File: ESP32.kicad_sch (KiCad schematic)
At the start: 16 parts, among them J24 Conn_01x02_Pin, J25 Conn_01x04_Pin, J26 Conn_01x02_Pin, J27 TC0203620000G, SW1 SW_Omron_B3FS, U2 ESP32-C3-WROOM-02

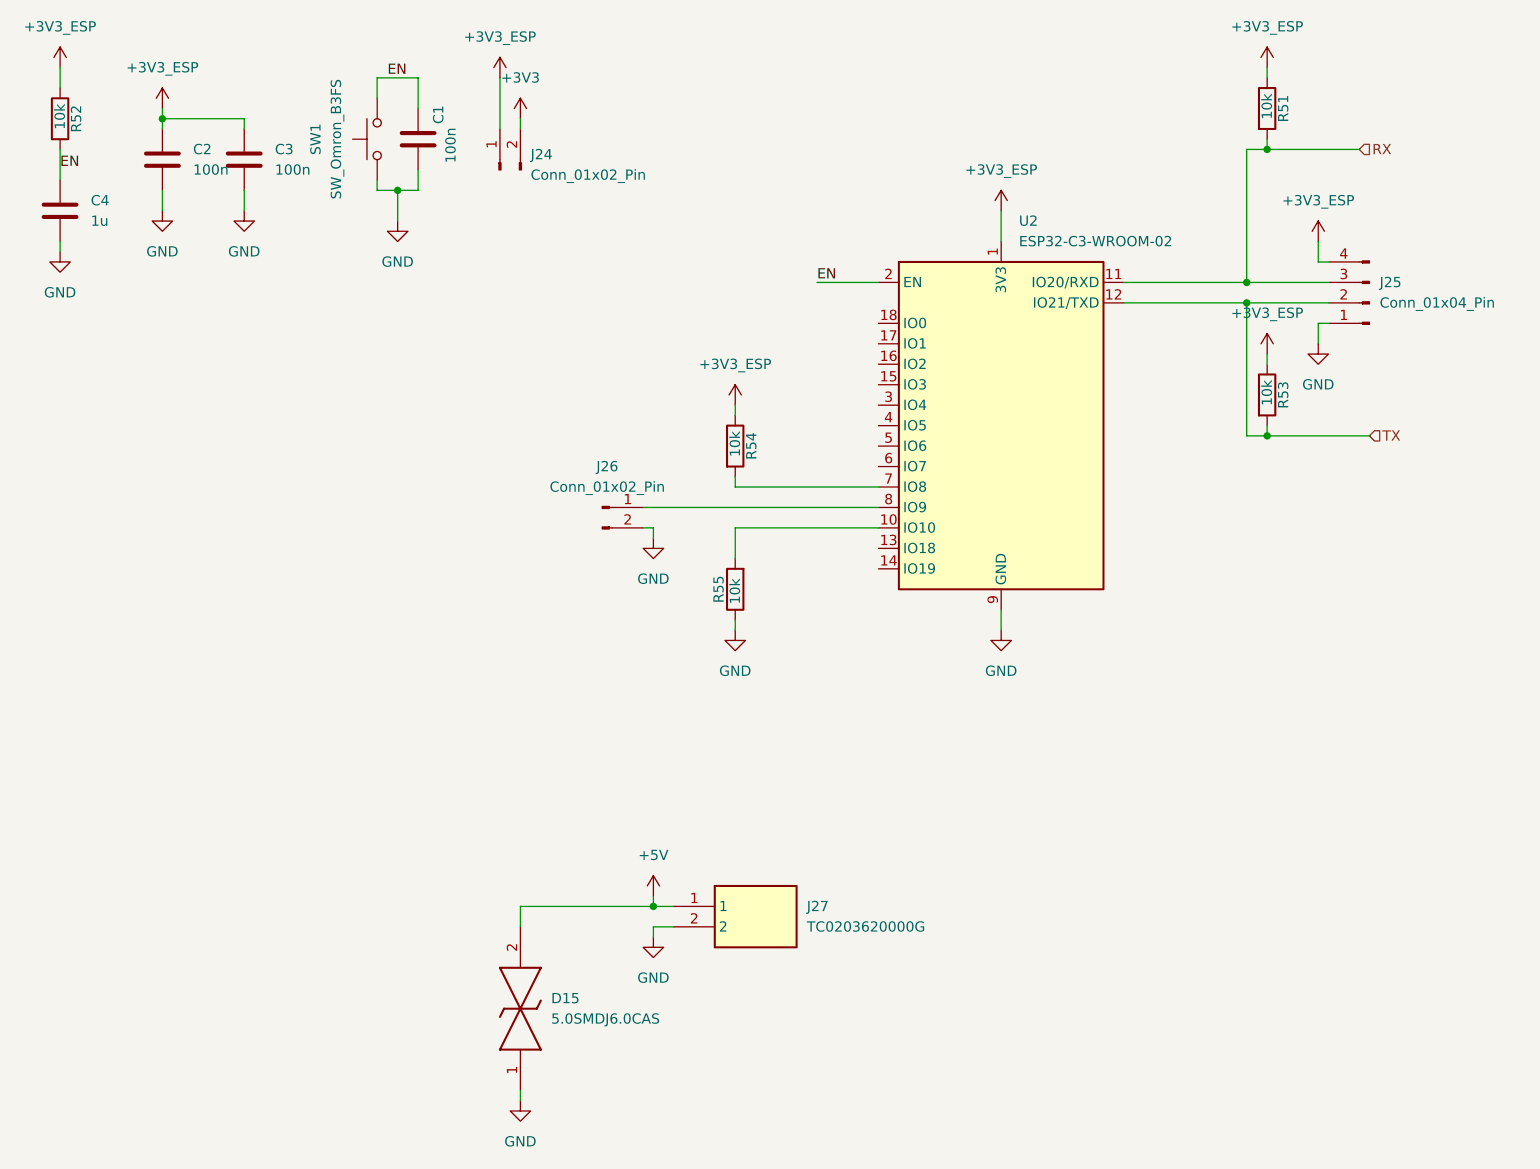
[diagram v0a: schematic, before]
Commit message: relay placment
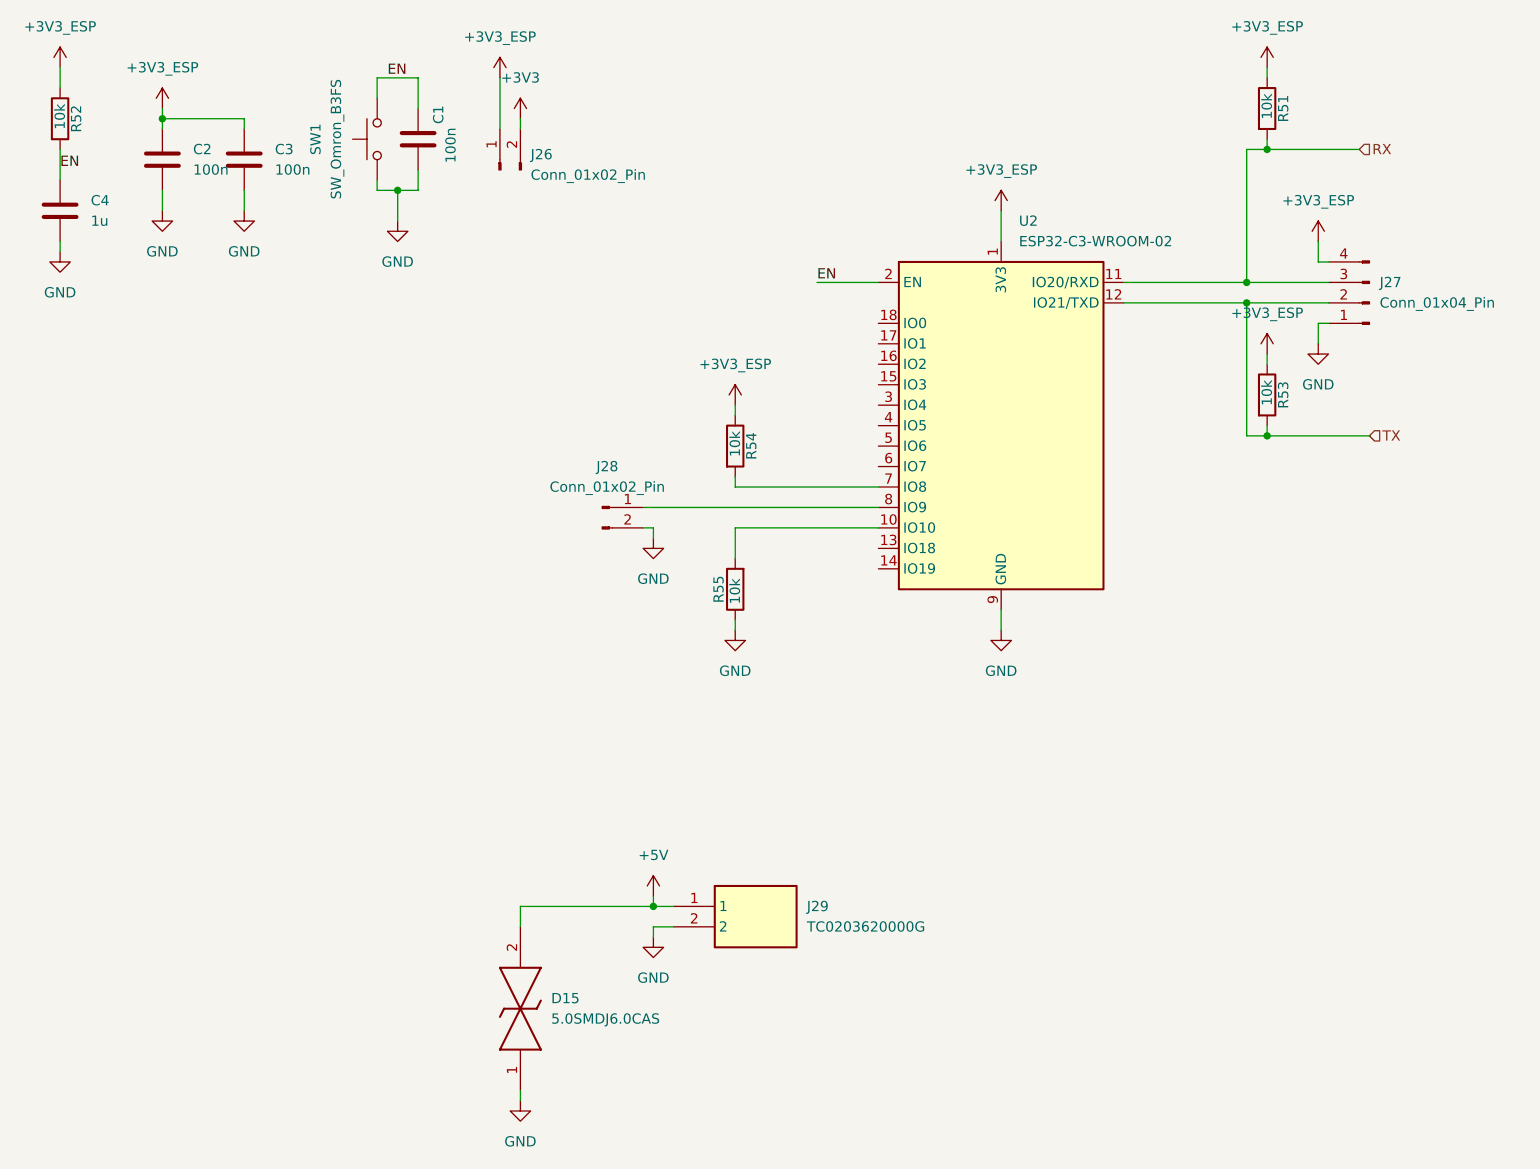
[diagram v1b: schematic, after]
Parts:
- renumbered J24 to J26, J25 to J27, J26 to J28, J27 to J29
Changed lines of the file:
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@@
 		(dnp no)
 		(fields_autoplaced yes)
-		(property "Reference" "J25"
+		(property "Reference" "J27"
 			(at 185.42 48.2599 0)
 			(effects
@@
 			(project ""
 				(path "/68de2dd7-8f08-479b-94c5-c7847794fd33/52852d8d-0d14-4226-9b6c-d04fc3c95df9"
-					(reference "J25")
+					(reference "J27")
 					(unit 1)
 				)
@@
 		(dnp no)
 		(fields_autoplaced yes)
-		(property "Reference" "#PWR0143"
+		(property "Reference" "#PWR0114"
 			(at 95.25 86.36 0)
 			(effects
@@
 			(project "home_auto"
 				(path "/68de2dd7-8f08-479b-94c5-c7847794fd33/52852d8d-0d14-4226-9b6c-d04fc3c95df9"
-					(reference "#PWR0143")
+					(reference "#PWR0114")
 					(unit 1)
 				)
@@
 		(dnp no)
 		(fields_autoplaced yes)
-		(property "Reference" "#PWR0145"
+		(property "Reference" "#PWR0116"
 			(at 138.43 97.79 0)
 			(effects
@@
 			(project "home_auto"
 				(path "/68de2dd7-8f08-479b-94c5-c7847794fd33/52852d8d-0d14-4226-9b6c-d04fc3c95df9"
-					(reference "#PWR0145")
+					(reference "#PWR0116")
 					(unit 1)
 				)
@@
 		(dnp no)
 		(fields_autoplaced yes)
-		(property "Reference" "#PWR0139"
+		(property "Reference" "#PWR0110"
 			(at 21.59 50.8 0)
 			(effects
@@
 			(project "home_auto"
 				(path "/68de2dd7-8f08-479b-94c5-c7847794fd33/52852d8d-0d14-4226-9b6c-d04fc3c95df9"
-					(reference "#PWR0139")
+					(reference "#PWR0110")
 					(unit 1)
 				)
@@
 		(dnp no)
 		(fields_autoplaced yes)
-		(property "Reference" "#PWR0129"
+		(property "Reference" "#PWR0100"
 			(at 21.59 25.4 0)
 			(effects
@@
 			(project "home_auto"
 				(path "/68de2dd7-8f08-479b-94c5-c7847794fd33/52852d8d-0d14-4226-9b6c-d04fc3c95df9"
-					(reference "#PWR0129")
+					(reference "#PWR0100")
 					(unit 1)
 				)
@@
 		(dnp no)
 		(fields_autoplaced yes)
-		(property "Reference" "#PWR0137"
+		(property "Reference" "#PWR0108"
 			(at 63.5 46.99 0)
 			(effects
@@
 			(project "home_auto"
 				(path "/68de2dd7-8f08-479b-94c5-c7847794fd33/52852d8d-0d14-4226-9b6c-d04fc3c95df9"
-					(reference "#PWR0137")
+					(reference "#PWR0108")
 					(unit 1)
 				)
@@
 		(dnp no)
 		(fields_autoplaced yes)
-		(property "Reference" "#PWR0142"
+		(property "Reference" "#PWR0113"
 			(at 105.41 67.31 0)
 			(effects
@@
 			(project "home_auto"
 				(path "/68de2dd7-8f08-479b-94c5-c7847794fd33/52852d8d-0d14-4226-9b6c-d04fc3c95df9"
-					(reference "#PWR0142")
+					(reference "#PWR0113")
 					(unit 1)
 				)
@@
 		(dnp no)
 		(fields_autoplaced yes)
-		(property "Reference" "J27"
+		(property "Reference" "J29"
 			(at 114.3 125.7299 0)
 			(effects
@@
 			(project "home_auto"
 				(path "/68de2dd7-8f08-479b-94c5-c7847794fd33/52852d8d-0d14-4226-9b6c-d04fc3c95df9"
-					(reference "J27")
+					(reference "J29")
 					(unit 1)
 				)
@@
 		(dnp no)
 		(fields_autoplaced yes)
-		(property "Reference" "#PWR0132"
+		(property "Reference" "#PWR0103"
 			(at 34.29 30.48 0)
 			(effects
@@
 			(project "home_auto"
 				(path "/68de2dd7-8f08-479b-94c5-c7847794fd33/52852d8d-0d14-4226-9b6c-d04fc3c95df9"
-					(reference "#PWR0132")
+					(reference "#PWR0103")
 					(unit 1)
 				)
@@
 		(dnp no)
 		(fields_autoplaced yes)
-		(property "Reference" "#PWR0144"
+		(property "Reference" "#PWR0115"
 			(at 105.41 97.79 0)
 			(effects
@@
 			(project "home_auto"
 				(path "/68de2dd7-8f08-479b-94c5-c7847794fd33/52852d8d-0d14-4226-9b6c-d04fc3c95df9"
-					(reference "#PWR0144")
+					(reference "#PWR0115")
 					(unit 1)
 				)
@@
 		(dnp no)
 		(fields_autoplaced yes)
-		(property "Reference" "#PWR0134"
+		(property "Reference" "#PWR0105"
 			(at 34.29 45.72 0)
 			(effects
@@
 			(project "home_auto"
 				(path "/68de2dd7-8f08-479b-94c5-c7847794fd33/52852d8d-0d14-4226-9b6c-d04fc3c95df9"
-					(reference "#PWR0134")
+					(reference "#PWR0105")
 					(unit 1)
 				)
@@
 		(dnp no)
 		(fields_autoplaced yes)
-		(property "Reference" "#PWR0138"
+		(property "Reference" "#PWR0109"
 			(at 177.8 46.99 0)
 			(effects
@@
 			(project "home_auto"
 				(path "/68de2dd7-8f08-479b-94c5-c7847794fd33/52852d8d-0d14-4226-9b6c-d04fc3c95df9"
-					(reference "#PWR0138")
+					(reference "#PWR0109")
 					(unit 1)
 				)
@@
 		(dnp no)
 		(fields_autoplaced yes)
-		(property "Reference" "#PWR0133"
+		(property "Reference" "#PWR0104"
 			(at 78.74 31.75 0)
 			(effects
@@
 			(project "home_auto"
 				(path "/68de2dd7-8f08-479b-94c5-c7847794fd33/52852d8d-0d14-4226-9b6c-d04fc3c95df9"
-					(reference "#PWR0133")
+					(reference "#PWR0104")
 					(unit 1)
 				)
@@
 		(dnp no)
 		(fields_autoplaced yes)
-		(property "Reference" "#PWR0130"
+		(property "Reference" "#PWR0101"
 			(at 171.45 25.4 0)
 			(effects
@@
 			(project "home_auto"
 				(path "/68de2dd7-8f08-479b-94c5-c7847794fd33/52852d8d-0d14-4226-9b6c-d04fc3c95df9"
-					(reference "#PWR0130")
+					(reference "#PWR0101")
 					(unit 1)
 				)
@@
 		(dnp no)
 		(fields_autoplaced yes)
-		(property "Reference" "#PWR0135"
+		(property "Reference" "#PWR0106"
 			(at 44.45 45.72 0)
 			(effects
@@
 			(project "home_auto"
 				(path "/68de2dd7-8f08-479b-94c5-c7847794fd33/52852d8d-0d14-4226-9b6c-d04fc3c95df9"
-					(reference "#PWR0135")
+					(reference "#PWR0106")
 					(unit 1)
 				)
@@
 		(dnp no)
 		(fields_autoplaced yes)
-		(property "Reference" "#PWR0136"
+		(property "Reference" "#PWR0107"
 			(at 138.43 43.18 0)
 			(effects
@@
 			(project "home_auto"
 				(path "/68de2dd7-8f08-479b-94c5-c7847794fd33/52852d8d-0d14-4226-9b6c-d04fc3c95df9"
-					(reference "#PWR0136")
+					(reference "#PWR0107")
 					(unit 1)
 				)
@@
 		(dnp no)
 		(fields_autoplaced yes)
-		(property "Reference" "#PWR0146"
+		(property "Reference" "#PWR0117"
 			(at 95.25 128.27 0)
 			(effects
@@
 			(project "home_auto"
 				(path "/68de2dd7-8f08-479b-94c5-c7847794fd33/52852d8d-0d14-4226-9b6c-d04fc3c95df9"
-					(reference "#PWR0146")
+					(reference "#PWR0117")
 					(unit 1)
 				)
@@
 		(dnp no)
 		(fields_autoplaced yes)
-		(property "Reference" "J26"
+		(property "Reference" "J28"
 			(at 89.535 71.12 0)
 			(effects
@@
 			(project ""
 				(path "/68de2dd7-8f08-479b-94c5-c7847794fd33/52852d8d-0d14-4226-9b6c-d04fc3c95df9"
-					(reference "J26")
+					(reference "J28")
 					(unit 1)
 				)
@@
 		(dnp no)
 		(fields_autoplaced yes)
-		(property "Reference" "#PWR0148"
+		(property "Reference" "#PWR0119"
 			(at 78.74 156.21 0)
 			(effects
@@
 			(project "home_auto"
 				(path "/68de2dd7-8f08-479b-94c5-c7847794fd33/52852d8d-0d14-4226-9b6c-d04fc3c95df9"
-					(reference "#PWR0148")
+					(reference "#PWR0119")
 					(unit 1)
 				)
@@
 		(dnp no)
 		(fields_autoplaced yes)
-		(property "Reference" "#PWR0140"
+		(property "Reference" "#PWR0111"
 			(at 177.8 62.23 0)
 			(effects
@@
 			(project "home_auto"
 				(path "/68de2dd7-8f08-479b-94c5-c7847794fd33/52852d8d-0d14-4226-9b6c-d04fc3c95df9"
-					(reference "#PWR0140")
+					(reference "#PWR0111")
 					(unit 1)
 				)
@@
 		(dnp no)
 		(fields_autoplaced yes)
-		(property "Reference" "#PWR0141"
+		(property "Reference" "#PWR0112"
 			(at 171.45 60.96 0)
 			(effects
@@
 			(project "home_auto"
 				(path "/68de2dd7-8f08-479b-94c5-c7847794fd33/52852d8d-0d14-4226-9b6c-d04fc3c95df9"
-					(reference "#PWR0141")
+					(reference "#PWR0112")
 					(unit 1)
 				)
@@
 		(dnp no)
 		(fields_autoplaced yes)
-		(property "Reference" "#PWR0131"
+		(property "Reference" "#PWR0102"
 			(at 76.2 26.67 0)
 			(effects
@@
 			(project "home_auto"
 				(path "/68de2dd7-8f08-479b-94c5-c7847794fd33/52852d8d-0d14-4226-9b6c-d04fc3c95df9"
-					(reference "#PWR0131")
+					(reference "#PWR0102")
 					(unit 1)
 				)
@@
 		(dnp no)
 		(fields_autoplaced yes)
-		(property "Reference" "#PWR0147"
+		(property "Reference" "#PWR0118"
 			(at 95.25 135.89 0)
 			(effects
@@
 			(project "home_auto"
 				(path "/68de2dd7-8f08-479b-94c5-c7847794fd33/52852d8d-0d14-4226-9b6c-d04fc3c95df9"
-					(reference "#PWR0147")
+					(reference "#PWR0118")
 					(unit 1)
 				)
@@
 		(dnp no)
 		(fields_autoplaced yes)
-		(property "Reference" "J24"
+		(property "Reference" "J26"
 			(at 80.01 32.3849 90)
 			(effects
@@
 			(project "home_auto"
 				(path "/68de2dd7-8f08-479b-94c5-c7847794fd33/52852d8d-0d14-4226-9b6c-d04fc3c95df9"
-					(reference "J24")
+					(reference "J26")
 					(unit 1)
 				)

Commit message: filse fo JCL pcb generated
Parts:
- J27: footprint Connector_PinHeader_1.27mm:PinHeader_1x04_P1.27mm_Vertical -> Connector_PinHeader_2.54mm:PinHeader_1x04_P2.54mm_Vertical
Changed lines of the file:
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@@
 			)
 		)
-		(property "Footprint" "Connector_PinHeader_1.27mm:PinHeader_1x04_P1.27mm_Vertical"
+		(property "Footprint" "Connector_PinHeader_2.54mm:PinHeader_1x04_P2.54mm_Vertical"
 			(at 184.15 50.8 0)
 			(effects
